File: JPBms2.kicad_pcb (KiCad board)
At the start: 4 copper layers, 69 x 39 mm, 89 parts, among them J1 Conn_ARM_SWD_TagConnect_TC2030, J2 Barrel_Jack_MountingPin, Q1 AO3401A, Q10 AO3401A, Q11 2N7002, Q2 AO3401A, Q3 AO3400A, Q4 AO3400A, Q5 AO3401A, Q6 2N7002, Q7 2N7002, Q8 AO3401A, U1 ST715M25R, U2 STM32L053R8Tx, U3 ZXCT1107, U4 IRS2003, U5 IRS2003

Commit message: Routing
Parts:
- removed TP_A1, TP_B1: TestPoint, TestPoint:TestPoint_Loop_D2.60mm_Drill1.6mm_Beaded
- added TP5: TestPoint, TestPoint:TestPoint_Loop_D2.60mm_Drill1.6mm_Beaded, F.Cu at (130.0, 88.0)
- added TP6: TestPoint, TestPoint:TestPoint_Loop_D2.60mm_Drill1.6mm_Beaded, F.Cu at (135.0, 88.0)
- TP1: value TestPoint -> SOLAR_CUR
- TP2: value TestPoint -> GND
- TP3: value TestPoint -> +BATT
- TP4: value TestPoint -> VDD
- moved UART1 0.38 mm to (140.4, 65.5)
- moved R7 0.14 mm to (134.9, 82.3)
- moved C3 0.13 mm to (130.3, 82.3)
- moved C12 0.11 mm to (133.3, 82.3)
- moved R8 0.06 mm to (131.8, 82.3)
- turned C8 to 180 degrees
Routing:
- net /MCU/USART1_TX: track 0.00 -> 18.4 mm
- net /MCU/USART1_RX: track 0.00 -> 17.4 mm
- net /MCU/NRST: track 9.93 -> 0.00 mm, vias 1 -> 0
- net VDD: track 15.8 -> 6.49 mm
- net /MCU/SWDIO: track 5.09 -> 0.00 mm
- net /MCU/SWCLK: track 4.93 -> 0.02 mm, vias 1 -> 0

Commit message: Layout done
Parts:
- moved H3 3.85 mm to (161.0, 97.0)
- moved H2 3.79 mm to (100.0, 97.0)
- moved TP4 2.03 mm to (111.0, 65.0)
- moved TP3 1.81 mm to (103.5, 90.0)
- moved H1 1.04 mm to (161.0, 66.0)
- moved D7 0.93 mm to (134.9, 71.3)
- moved D8 0.93 mm to (134.9, 74.0)
- moved C10 0.85 mm to (132.7, 76.3), turned to 0 degrees
- moved R1 0.25 mm to (150.5, 64.3)
- moved R3 0.25 mm to (150.5, 68.2)
- moved C4 0.23 mm to (123.0, 80.3), turned to -90 degrees
- moved C12 0.20 mm to (133.3, 82.5)
- moved C3 0.20 mm to (130.3, 82.5)
- moved R7 0.20 mm to (134.9, 82.5)
- moved R8 0.20 mm to (131.8, 82.5)
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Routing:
- net GND: track 7.73 -> 76.5 mm, vias 0 -> 34
- net CELL_8V: track 0.00 -> 63.7 mm, vias 0 -> 4
- net CELL_4V: track 6.47 -> 62.4 mm, vias 0 -> 4
- net /MCU/NRST: track 0.00 -> 41.7 mm
- net /MCU/LED_ERROR: track 0.00 -> 37.2 mm, vias 0 -> 2
- net /MCU/LED_ON: track 0.00 -> 34.6 mm, vias 0 -> 4
- net /MCU/LED_ACTIVE: track 0.00 -> 34.5 mm, vias 0 -> 2
- net DD_BOT_B: track 0.00 -> 34.4 mm, vias 0 -> 2
- net VDD: track 6.49 -> 40.1 mm, vias 0 -> 13
- net DD_TOP_B: track 0.00 -> 31.7 mm, vias 0 -> 2
- net /MCU/SWDIO: track 0.00 -> 25.4 mm, vias 0 -> 2
- net /MCU/SWCLK: track 0.02 -> 24.6 mm
- net DD_TOP_A: track 0.00 -> 23.8 mm, vias 0 -> 2
- net DD_BOT_A: track 0.00 -> 22.8 mm, vias 0 -> 2
- net NBAL_3: track 0.00 -> 21.7 mm, vias 0 -> 2
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- added copper zone on In1.Cu, net GND
- added copper zone on In2.Cu, net VDD

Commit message: bom pt1
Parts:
- C6: footprint Capacitor_SMD:C_0805_2012Metric -> Capacitor_SMD:C_1206_3216Metric
- moved C6 0.53 mm to (116.3, 73.2)
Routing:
- net GND: track 76.5 -> 77.6 mm
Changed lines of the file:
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@@
 			)
 		)
+		(property "LCSC_Code" "C1634"
+			(at 0 0 180)
+			(unlocked yes)
+			(layer "F.Fab")
+			(hide yes)
+			(effects
+				(font
+					(size 1 1)
+					(thickness 0.15)
+				)
+			)
+		)
 		(property ki_fp_filters "C_*")
 		(sheetname "Power")
@@
 			)
 		)
+		(property "LCSC_Code" "C157925"
+			(at 0 0 -90)
+			(unlocked yes)
+			(layer "F.Fab")
+			(hide yes)
+			(effects
+				(font
+					(size 1 1)
+					(thickness 0.15)
+				)
+			)
+		)
 		(property ki_fp_filters "Connector*:*_1x??_*")
 		(sheetname "Power")
@@
 			)
 		)
-		(property "LCSC_Code" "C15850"
+		(property "LCSC_Code" "C13585"
 			(at 0 0 -90)
 			(unlocked yes)
@@
 		)
 	)
-	(footprint "Capacitor_SMD:C_0805_2012Metric"
+	(footprint "Capacitor_SMD:C_1206_3216Metric"
 		(layer "F.Cu")
-		(at 116.459 73.726 90)
-		(descr "Capacitor SMD 0805 (2012 Metric), square (rectangular) end terminal, IPC_7351 nominal, (Body size source: IPC-SM-782 page 76, https://www.pcb-3d.com/wordpress/wp-content/uploads/ipc-sm-782a_amendment_1_and_2.pdf, https://docs.google.com/spreadsheets/d/1BsfQQcO9C6DZCsRaXUlFlo91Tg2WpOkGARC1WS5S8t0/edit?usp=sharing), generated with kicad-footprint-generator")
+		(at 116.336748 73.214253 90)
+		(descr "Capacitor SMD 1206 (3216 Metric), square (rectangular) end terminal, IPC_7351 nominal, (Body size source: IPC-SM-782 page 76, https://www.pcb-3d.com/wordpress/wp-content/uploads/ipc-sm-782a_amendment_1_and_2.pdf), generated with kicad-footprint-generator")
 		(tags "capacitor")
 		(property "Reference" "C6"
-			(at 2.726 0.541 90)
+			(at 3.226 0.041 180)
 			(layer "F.SilkS")
 			(effects
@@
 		)
 		(property "Value" "10u"
-			(at 0 1.68 -90)
+			(at 0 1.85 90)
 			(layer "F.Fab")
 			(effects
@@
 			)
 		)
-		(property "Footprint" "Capacitor_SMD:C_0805_2012Metric"
+		(property "Footprint" "Capacitor_SMD:C_1206_3216Metric"
 			(at 0 0 90)
 			(unlocked yes)
@@
 			)
 		)
-		(property "LCSC_Code" "C15850"
+		(property "LCSC_Code" "C13585"
 			(at 0 0 90)
 			(unlocked yes)
@@
 		(attr smd)
 		(fp_line
-			(start -0.261252 -0.735)
-			(end 0.261252 -0.735)
+			(start -0.711252 -0.91)
+			(end 0.711252 -0.91)
 			(stroke
 				(width 0.12)
@@
 		)
 		(fp_line
-			(start -0.261252 0.735)
-			(end 0.261252 0.735)
+			(start -0.711252 0.91)
+			(end 0.711252 0.91)
 			(stroke
 				(width 0.12)
@@
 		)
 		(fp_line
-			(start 1.7 -0.98)
-			(end 1.7 0.98)
+			(start 2.3 -1.15)
+			(end 2.3 1.15)
 			(stroke
 				(width 0.05)
@@
 		)
 		(fp_line
-			(start -1.7 -0.98)
-			(end 1.7 -0.98)
+			(start -2.3 -1.15)
+			(end 2.3 -1.15)
 			(stroke
 				(width 0.05)
@@
 		)
 		(fp_line
-			(start 1.7 0.98)
-			(end -1.7 0.98)
+			(start 2.3 1.15)
+			(end -2.3 1.15)
 			(stroke
 				(width 0.05)
@@
 		)
 		(fp_line
-			(start -1.7 0.98)
-			(end -1.7 -0.98)
+			(start -2.3 1.15)
+			(end -2.3 -1.15)
 			(stroke
 				(width 0.05)
@@
 		)
 		(fp_line
-			(start 1 -0.625)
-			(end 1 0.625)
+			(start 1.6 -0.8)
+			(end 1.6 0.8)
 			(stroke
 				(width 0.1)
@@
 		)
 		(fp_line
-			(start -1 -0.625)
-			(end 1 -0.625)
+			(start -1.6 -0.8)
+			(end 1.6 -0.8)
 			(stroke
 				(width 0.1)
@@
 		)
 		(fp_line
-			(start 1 0.625)
-			(end -1 0.625)
+			(start 1.6 0.8)
+			(end -1.6 0.8)
 			(stroke
 				(width 0.1)
@@
 		)
 		(fp_line
-			(start -1 0.625)
-			(end -1 -0.625)
+			(start -1.6 0.8)
+			(end -1.6 -0.8)
 			(stroke
 				(width 0.1)
@@
 		)
 		(fp_text user "${REFERENCE}"
-			(at 0 0 -90)
+			(at 0 0 90)
 			(layer "F.Fab")
 			(effects
 				(font
-					(size 0.5 0.5)
-					(thickness 0.08)
+					(size 0.8 0.8)
+					(thickness 0.12)
 				)
 			)
 		)
 		(pad "1" smd roundrect
-			(at -0.95 0 90)
-			(size 1 1.45)
+			(at -1.475 0 90)
+			(size 1.15 1.8)
 			(layers "F.Cu" "F.Paste" "F.Mask")
-			(roundrect_rratio 0.25)
+			(roundrect_rratio 0.217391)
 			(net 2 "VDD")
 			(pintype "passive")
 		)
 		(pad "2" smd roundrect
-			(at 0.95 0 90)
-			(size 1 1.45)
+			(at 1.475 0 90)
+			(size 1.15 1.8)
 			(layers "F.Cu" "F.Paste" "F.Mask")
-			(roundrect_rratio 0.25)
+			(roundrect_rratio 0.217391)
 			(net 1 "GND")
 			(pintype "passive")
 		)
-		(model "${KICAD8_3DMODEL_DIR}/Capacitor_SMD.3dshapes/C_0805_2012Metric.wrl"
+		(model "${KICAD8_3DMODEL_DIR}/Capacitor_SMD.3dshapes/C_1206_3216Metric.wrl"
 			(offset
 				(xyz 0 0 0)
@@
 			)
 		)
+		(property "LCSC_Code" "C234195"
+			(at 0 0 0)
+			(unlocked yes)
+			(layer "F.Fab")
+			(hide yes)
+			(effects
+				(font
+					(size 1 1)
+					(thickness 0.15)
+				)
+			)
+		)
 		(property ki_fp_filters "Connector*:*_1x??_*")
 		(sheetname "MCU")
@@
 			)
 		)
-		(property "LCSC_Code" "C15850"
+		(property "LCSC_Code" "C13585"
 			(at 0 0 90)
 			(unlocked yes)
@@
 	)
 	(segment
+		(start 116.336748 71.739253)
+		(end 116.336748 72.653748)
+		(width 0.2)
+		(layer "F.Cu")
+		(net 1)
+	)
+	(segment
 		(start 122.53 64.545)
 		(end 122.53 65.53)
@@
 	)
 	(segment
+		(start 116.336748 72.653748)
+		(end 116.459 72.776)
+		(width 0.2)
+		(layer "F.Cu")
+		(net 1)
+	)
+	(segment
 		(start 139.001 74.422)
 		(end 140.335 74.422)
@@
 	)
 	(segment
-		(start 116.459 74.676)
-		(end 115.324 74.676)
-		(width 0.2)
-		(layer "F.Cu")
-		(net 2)
-	)
-	(segment
 		(start 112.060426 72.4075)
 		(end 112.117926 72.35)
@@
 	)
 	(segment
-		(start 116.7 74.435)
-		(end 116.459 74.676)
-		(width 0.2)
-		(layer "F.Cu")
-		(net 2)
-	)
-	(segment
 		(start 155.67 64.33)
 		(end 156.5 63.5)
@@
 	)
 	(segment
-		(start 136.032 79.994)
-		(end 136.006 79.994)
+		(start 118.28 74.435)
+		(end 115.564968 74.435)
 		(width 0.2)
 		(layer "F.Cu")
@@
 	)
 	(segment
-		(start 115.324 74.676)
-		(end 115 75)
+		(start 136.032 79.994)
+		(end 136.006 79.994)
 		(width 0.2)
 		(layer "F.Cu")
@@
 	)
 	(segment
+		(start 115.564968 74.435)
+		(end 114.999968 75)
+		(width 0.2)
+		(layer "F.Cu")
+		(net 2)
+	)
+	(segment
 		(start 101.64755 66.08245)
 		(end 104.41755 66.08245)
@@
 	)
 	(segment
-		(start 118.28 74.435)
-		(end 116.7 74.435)
-		(width 0.2)
-		(layer "F.Cu")
-		(net 2)
-	)
-	(segment
 		(start 131.455 66.47)
 		(end 132.64 66.47)
@@
 	)
 	(via
-		(at 115 75)
+		(at 114.999968 75)
 		(size 0.6)
 		(drill 0.3)

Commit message: Assigning PNs
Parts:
- L1: value 220uH -> 22uH
- R11, R12, R13, R14: value 50 -> 75
- R29: value 160k -> 150k

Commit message: slight changes
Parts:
- removed C3: .1u, Capacitor_SMD:C_0603_1608Metric
- C1: value 470n -> 10u
- C16, C17: value .1u -> 1u
- C2: value 470n -> 47u
- moved C10 3.20 mm to (133.6, 73.2), turned to -90 degrees
- moved TP3 2.12 mm to (104.2, 88.0)
- moved TP2 2.01 mm to (104.2, 73.8)
- moved C18 1.65 mm to (142.1, 72.1)
- moved C19 1.65 mm to (142.1, 75.4)
- moved D7 1.65 mm to (136.5, 71.4)
- moved D8 1.65 mm to (136.5, 74.0)
- moved R27 1.65 mm to (139.9, 71.1)
- moved R28 1.65 mm to (139.8, 72.8)
- moved R29 1.65 mm to (139.9, 76.1)
- moved R30 1.65 mm to (139.8, 74.5)
- moved Q4 0.89 mm to (139.6, 96.4)
- moved C15 0.43 mm to (153.5, 86.5)
- moved C14 0.30 mm to (153.5, 77.5)
- moved Q3 0.18 mm to (126.2, 96.4)
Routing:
- net CELL_4V: track 62.4 -> 85.7 mm, vias 4 -> 3
- net VDD: track 40.1 -> 34.3 mm
- net GND: track 77.6 -> 74.8 mm
- net CELL_8V: track 63.7 -> 61.1 mm
- net CELL_4V_ADC: track 9.89 -> 12.1 mm
- net Net-(BAL1-Pin_4): track 9.49 -> 7.78 mm
- net CELL_8V_ADC: track 12.4 -> 13.6 mm
- net VSOLAR: track 53.2 -> 52.3 mm
- net DD_BOT_B: track 34.4 -> 35.0 mm

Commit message: New design and layout
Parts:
- added R31: 220k, Resistor_SMD:R_0402_1005Metric, F.Cu at (133.2, 83.7)
- added R32: 220k, Resistor_SMD:R_0402_1005Metric, F.Cu at (134.2, 83.7)
- added R33: 47.5k, Resistor_SMD:R_0402_1005Metric, F.Cu at (133.2, 81.8)
- added R34: 47.5k, Resistor_SMD:R_0402_1005Metric, F.Cu at (134.2, 81.8)
- added R35: 220k, Resistor_SMD:R_0402_1005Metric, F.Cu at (139.8, 74.3)
- added R36: 220k, Resistor_SMD:R_0402_1005Metric, F.Cu at (138.8, 74.3)
- added R37: 47.5k, Resistor_SMD:R_0402_1005Metric, F.Cu at (144.0, 74.4)
- added R38: 47.5k, Resistor_SMD:R_0402_1005Metric, F.Cu at (143.0, 74.4)
- BAL1: value Conn_01x04 -> Conn_01x04 JST-XH
- C12, C13, C18, C19: value 1n -> .1u
- D1: value LED -> LED_G
- D2: value LED -> LED_Y
- D3: value LED -> LED_R
- R10: value 39k -> 47.5k; footprint Resistor_SMD:R_0603_1608Metric -> Resistor_SMD:R_0402_1005Metric
- R27: value 390k -> 220k; footprint Resistor_SMD:R_0603_1608Metric -> Resistor_SMD:R_0402_1005Metric
- R28: value 150k -> 220k; footprint Resistor_SMD:R_0603_1608Metric -> Resistor_SMD:R_0402_1005Metric
- R29: value 150k -> 47.5k; footprint Resistor_SMD:R_0603_1608Metric -> Resistor_SMD:R_0402_1005Metric
- R30, R9: value 200k -> 47.5k; footprint Resistor_SMD:R_0603_1608Metric -> Resistor_SMD:R_0402_1005Metric
- R4: value 0.25 -> 0.1
- R6: value 1.2k -> 3k
- R7: value 200k -> 220k; footprint Resistor_SMD:R_0603_1608Metric -> Resistor_SMD:R_0402_1005Metric
- R8: value 39k -> 220k; footprint Resistor_SMD:R_0603_1608Metric -> Resistor_SMD:R_0402_1005Metric
- UART1: value Conn_01x04 -> Conn_01x04 Picoblade
- moved R6 14.1 mm to (137.6, 79.0), turned to -90 degrees
- moved R9 5.89 mm to (130.4, 81.8), turned to -90 degrees
- moved R29 5.64 mm to (143.0, 71.4), turned to -90 degrees
- moved R7 5.60 mm to (129.4, 83.7)
- moved R30 5.17 mm to (144.0, 71.4), turned to -90 degrees
- moved C12 5.15 mm to (128.2, 82.4), turned to 90 degrees
- moved C13 4.75 mm to (132.0, 82.4), turned to 90 degrees
- moved R10 3.50 mm to (129.4, 81.8), turned to -90 degrees
- moved D6 2.81 mm to (132.6, 79.0)
- moved D5 2.79 mm to (129.8, 79.0)
- moved C4 2.18 mm to (124.4, 78.6)
- moved R8 1.85 mm to (130.4, 83.7)
- moved R28 1.40 mm to (139.8, 71.4), turned to -90 degrees
- moved R27 1.12 mm to (138.8, 71.4), turned to -90 degrees
- moved C19 1.08 mm to (141.6, 74.4)
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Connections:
- D1 pad 1: Net-(D1-K) -> GND
- D1 pad 2: VDD -> Net-(D1-A)
- D2 pad 1: Net-(D2-K) -> GND
- D2 pad 2: VDD -> Net-(D2-A)
- D3 pad 1: Net-(D3-K) -> GND
- D3 pad 2: VDD -> Net-(D3-A)
- Q1 pad 2: /BuckBoost/VS_A -> +BATT
- Q1 pad 3: +BATT -> /BuckBoost/VS_A
- Q10 pad 2: Net-(Q10-S) -> CELL_4V
- Q10 pad 3: CELL_4V -> Net-(Q10-D)
- Q2 pad 2: /BuckBoost/VS_B -> VSOLAR
- Q2 pad 3: VSOLAR -> /BuckBoost/VS_B
- Q5 pad 2: Net-(Q5-S) -> +BATT
- Q5 pad 3: +BATT -> Net-(Q5-D)
- Q8 pad 2: Net-(Q8-S) -> CELL_8V
- Q8 pad 3: CELL_8V -> Net-(Q8-D)
- R1 pad 2: Net-(D1-K) -> Net-(D1-A)
- R10 pad 2: VSOLAR_ADC -> VBATT_ADC
- R16 pad 1: Net-(Q5-S) -> Net-(Q5-D)
- R2 pad 2: Net-(D2-K) -> Net-(D2-A)
- R22 pad 1: Net-(Q8-S) -> Net-(Q8-D)
- R26 pad 1: Net-(Q10-S) -> Net-(Q10-D)
- R28 pad 1: GND -> CELL_8V
- R29 pad 1: CELL_4V -> GND
- R29 pad 2: CELL_4V_ADC -> CELL_8V_ADC
- R3 pad 2: Net-(D3-K) -> Net-(D3-A)
- R30 pad 2: CELL_4V_ADC -> CELL_8V_ADC
- R8 pad 1: GND -> +BATT
- R9 pad 1: VSOLAR -> GND
- R9 pad 2: VSOLAR_ADC -> VBATT_ADC
- U2 pad 14: VSOLAR_ADC -> VBATT_ADC
- U2 pad 15: VBATT_ADC -> VSOLAR_ADC
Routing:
- net VDD: track 34.3 -> 96.7 mm, vias 13 -> 10
- net /MCU/LED_ERROR: track 37.2 -> 0.00 mm, vias 2 -> 0
- net DD_BOT_B: track 35.0 -> 0.00 mm, vias 2 -> 0
- net /MCU/NRST: track 41.7 -> 12.0 mm
- net DD_TOP_A: track 23.8 -> 0.00 mm, vias 2 -> 0
- net DD_BOT_A: track 22.8 -> 0.00 mm, vias 2 -> 0
- net NBAL_3: track 21.7 -> 0.00 mm, vias 2 -> 0
- net CELL_4V: track 85.7 -> 66.8 mm, vias 3 -> 4
- net VSOLAR: track 52.3 -> 34.6 mm
- net NBAL_2: track 16.4 -> 0.00 mm, vias 2 -> 0
- net SOLAR_CURRENT_ADC: track 38.6 -> 54.5 mm, vias 2 -> 0
- net Net-(Q5-S): track 13.5 -> 0.00 mm
- net Net-(Q5-D): track 0.00 -> 11.6 mm
- net NBAL_1: track 9.98 -> 0.00 mm, vias 2 -> 0
- net Net-(Q8-S): track 8.52 -> 0.00 mm, vias 2 -> 0
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- added copper zone on In2.Cu, net GND
- removed copper zone on In2.Cu, net VDD
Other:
- board text added: "PozSolarChg v1.1"
- board text removed: "PozSolarChg v1.0"

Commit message: Finishing layout
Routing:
- net /MCU/LED_ERROR: track 0.00 -> 41.0 mm
- net DD_BOT_B: track 0.00 -> 38.7 mm, vias 0 -> 2
- net NBAL_3: track 0.00 -> 34.5 mm, vias 0 -> 4
- net DD_BOT_A: track 0.00 -> 32.7 mm, vias 0 -> 2
- net DD_TOP_A: track 0.00 -> 31.2 mm, vias 0 -> 2
- net NBAL_2: track 0.00 -> 29.7 mm, vias 0 -> 2
- net /MCU/NRST: track 12.0 -> 38.9 mm, vias 0 -> 2
- net NBAL_1: track 0.00 -> 11.3 mm
- net SOLAR_CURRENT_ADC: track 54.5 -> 61.8 mm
- net GND: track 80.4 -> 82.7 mm, vias 35 -> 59
- net DD_TOP_B: track 36.7 -> 35.3 mm
- net VDD: track 96.7 -> 98.1 mm
- net CELL_4V: track 66.8 -> 65.7 mm
- net CELL_8V: track 62.2 -> 61.5 mm

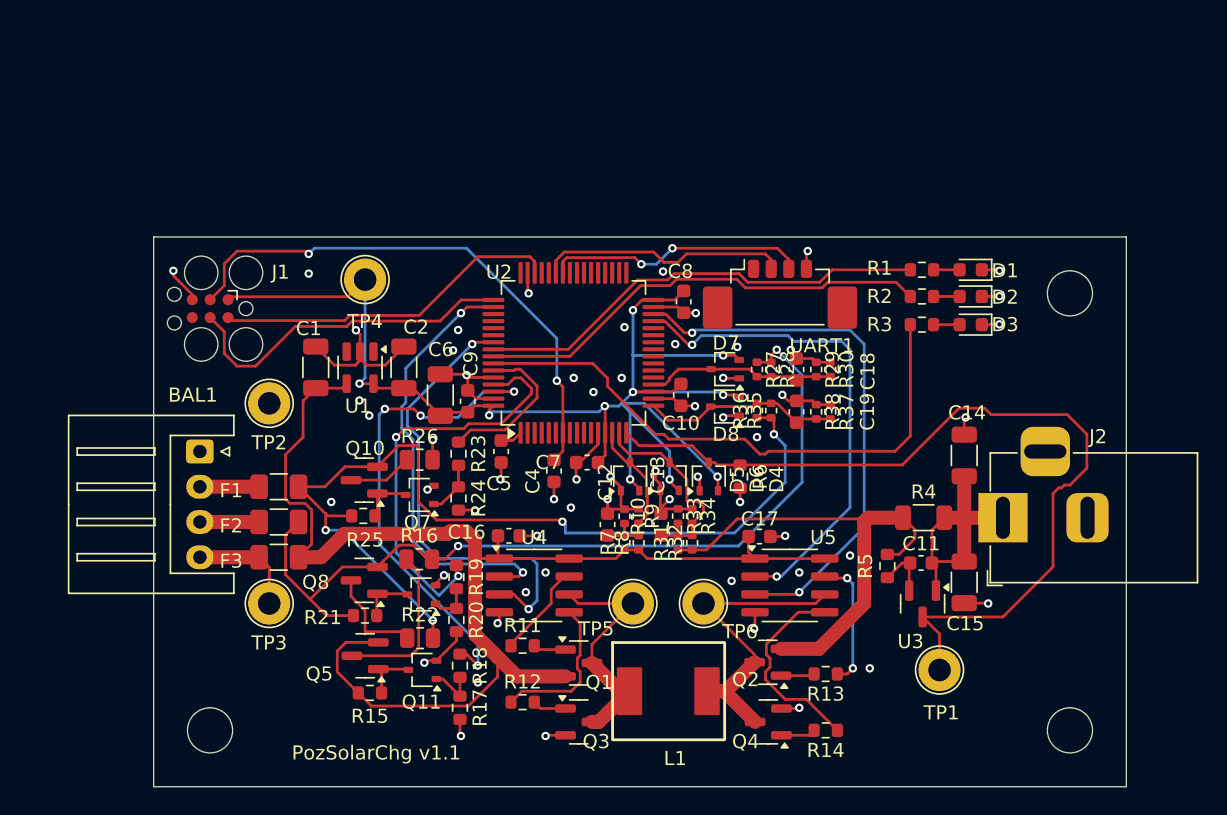
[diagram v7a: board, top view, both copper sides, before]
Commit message: Better balance resistors, fixes
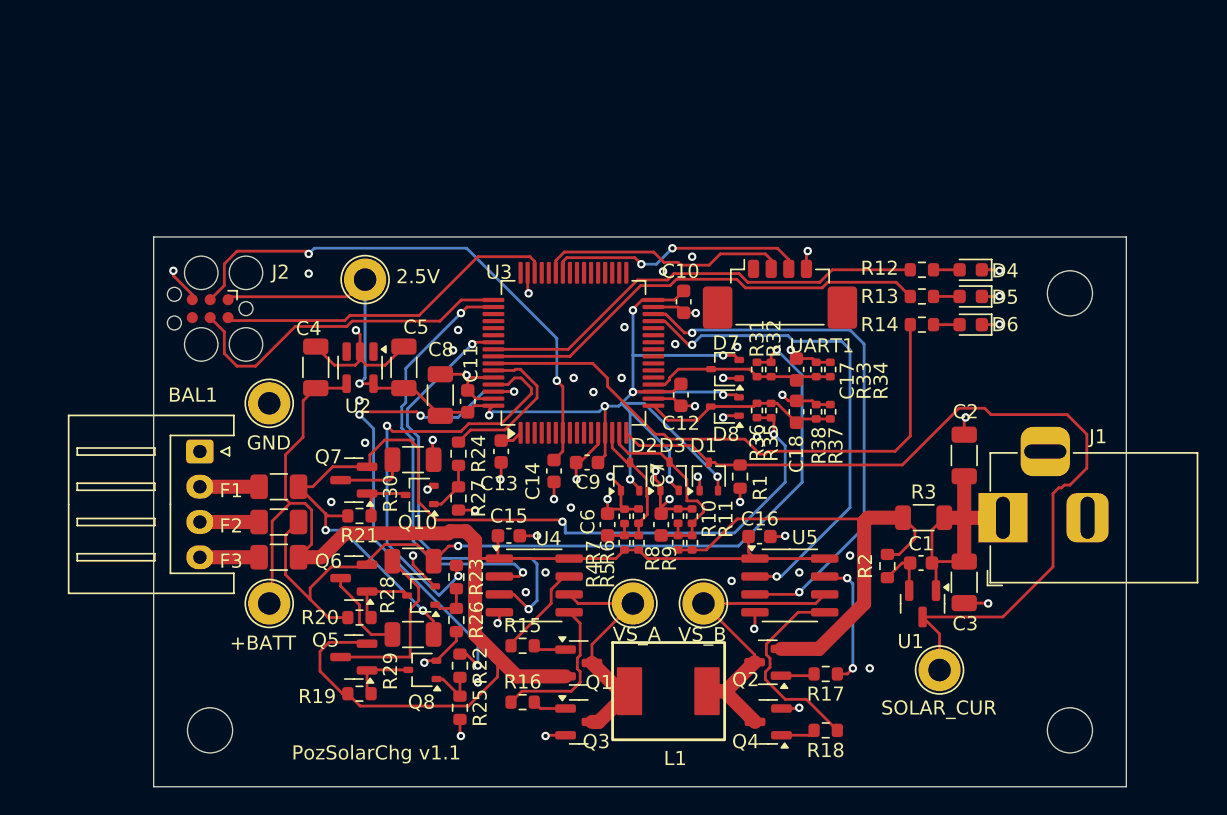
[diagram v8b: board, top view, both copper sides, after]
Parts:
- R28: renamed from R16; footprint Resistor_SMD:R_0805_2012Metric -> Resistor_SMD:R_1206_3216Metric
- R29: renamed from R22; footprint Resistor_SMD:R_0805_2012Metric -> Resistor_SMD:R_1206_3216Metric
- R30: renamed from R26; footprint Resistor_SMD:R_0805_2012Metric -> Resistor_SMD:R_1206_3216Metric
- moved Q5 0.81 mm to (110.2, 91.8)
- moved Q6 0.75 mm to (110.2, 86.2)
- moved R19 0.74 mm to (110.6, 94.4)
- moved Q7 0.74 mm to (110.2, 79.2)
- moved R29 0.56 mm to (114.4, 90.2)
- moved R30 0.47 mm to (114.4, 77.8)
- moved R28 0.46 mm to (114.4, 85.0)
- moved R20 0.42 mm to (110.6, 89.0)
- moved R21 0.27 mm to (110.6, 81.8)
- moved Q9 0.08 mm to (115.0, 87.4)
- renumbered C11 to C1, C8 to C10, C9 to C11, C10 to C12, C5 to C13, C4 to C14, C16 to C15, C17 to C16, C18 to C17, C19 to C18, C14 to C2, C15 to C3, C1 to C4, C2 to C5, C12 to C6, C13 to C7, C6 to C8, C7 to C9, D4 to D1, D5 to D2, D6 to D3, D1 to D4, D2 to D5, D3 to D6, J2 to J1, J1 to J2, Q7 to Q10, Q8 to Q6, Q10 to Q7, Q11 to Q8, Q6 to Q9, R6 to R1, R33 to R10, R34 to R11, R1 to R12, R2 to R13, R3 to R14, R11 to R15, R12 to R16, R13 to R17, R14 to R18, R15 to R19, R5 to R2, R21 to R20, R25 to R21, R18 to R22, R19 to R23, R23 to R24, R17 to R25, R20 to R26, R24 to R27, R4 to R3, R27 to R31, R28 to R32, R29 to R33, R30 to R34, R7 to R4, R8 to R5, R9 to R6, R10 to R7, R31 to R8, R32 to R9, TP2 to TP1, TP3 to TP2, TP1 to TP3, U3 to U1, U1 to U2, U2 to U3
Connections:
- TP2 pad 1: Net-(BAL1-Pin_4) -> +BATT
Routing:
- net +BATT: track 92.9 -> 102.2 mm
- net Net-(BAL1-Pin_4): track 7.78 -> 4.20 mm
- net GND: track 82.7 -> 84.7 mm, vias 59 -> 60
- net NBAL_3: track 34.5 -> 36.3 mm
- net NBAL_2: track 29.7 -> 31.4 mm
- net Net-(Q5-D): track 11.6 -> 12.9 mm
- net Net-(Q6-G): track 3.72 -> 4.94 mm
- net Net-(Q6-D): track 7.23 -> 6.40 mm
- net Net-(Q5-G): track 3.92 -> 4.71 mm
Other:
- board text added: "+BATT"
- board text added: "2.5V"
- board text added: "GND"
- board text added: "SOLAR_CUR"
- board text added: "VS_A"
- board text added: "VS_B"
